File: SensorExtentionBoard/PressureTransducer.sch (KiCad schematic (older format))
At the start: 13 parts, among them J501 Conn_01x03_Male, J502 Conn_01x03_Male, J503 Conn_01x03_Male, U501 ADS1015IDGS, U502 MCP4728

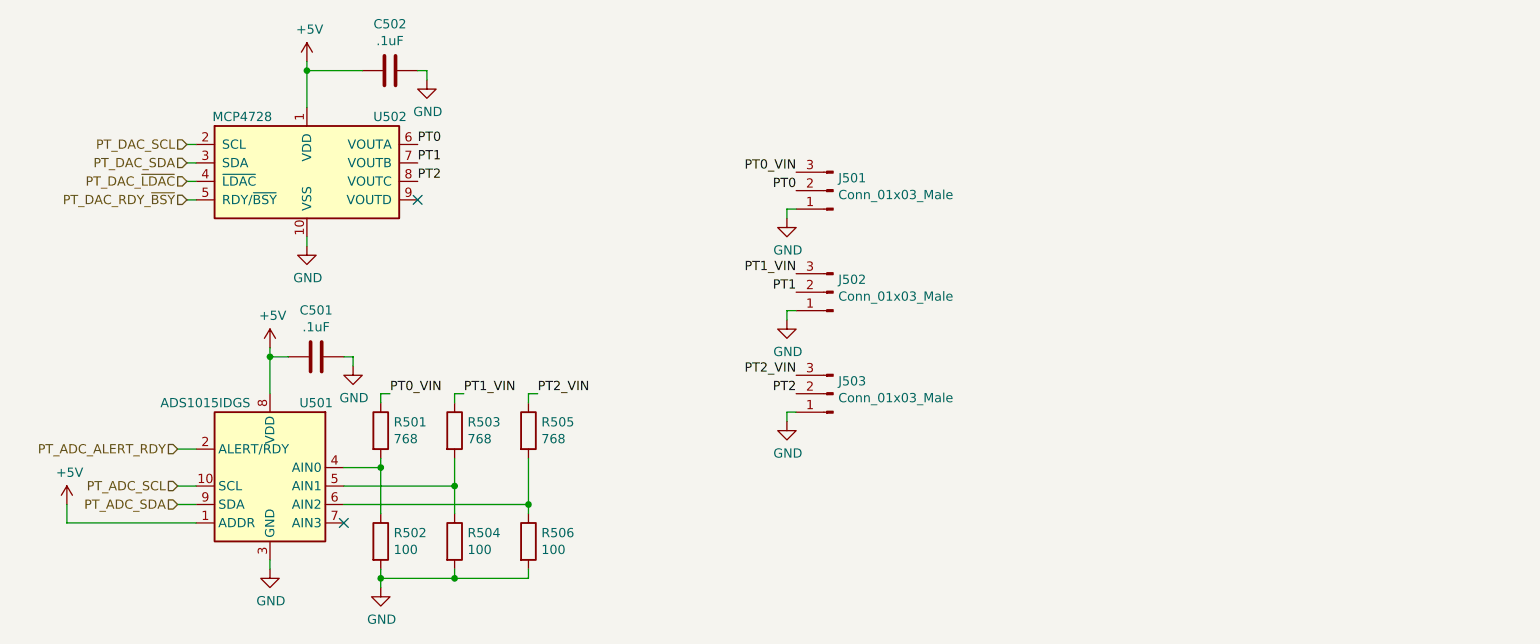
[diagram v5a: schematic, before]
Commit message: Added header for programming the EEPROM memory on the SEB
Adding this header may allow the test rig to load new memory configs
onto the SEB under test prior to running tests. This will allow
greater ability for automation of testing when the new software
requires a change to the config onboard the SEB.
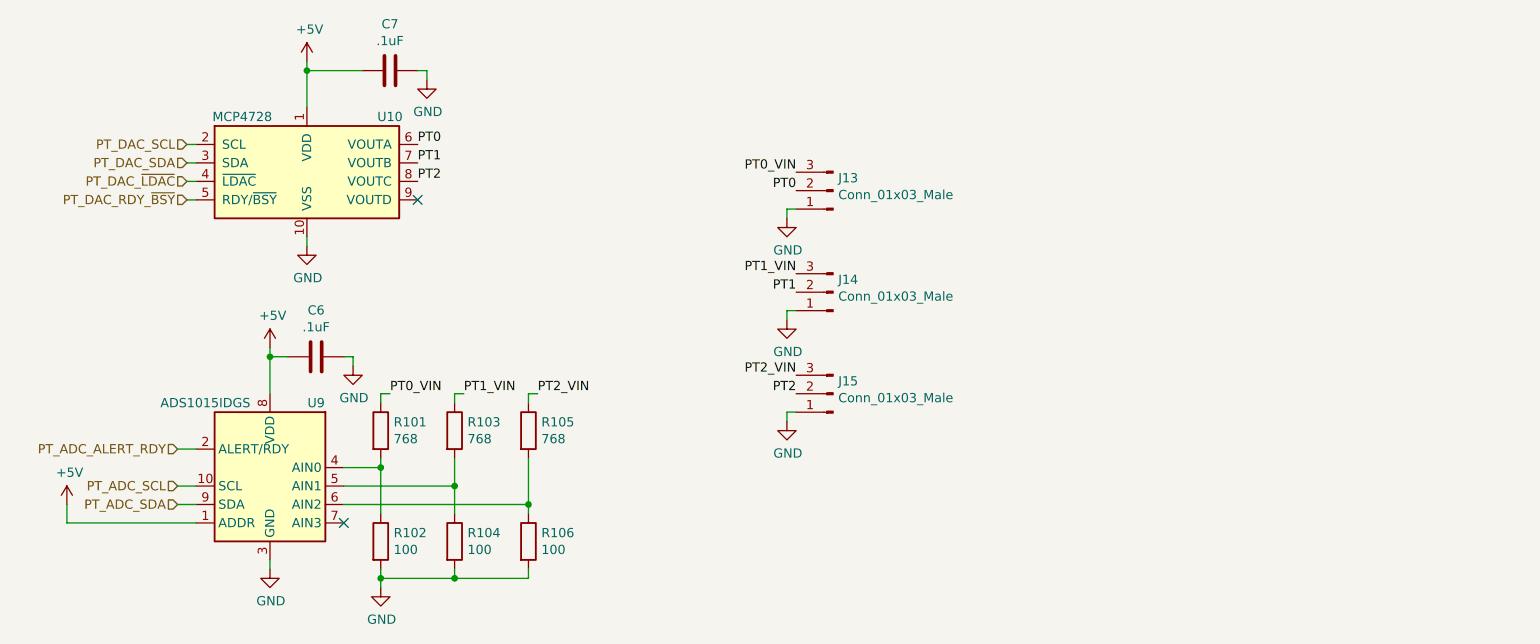
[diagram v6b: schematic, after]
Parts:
- renumbered C501 to C6, C502 to C7, J501 to J13, J502 to J14, J503 to J15, R501 to R101, R502 to R102, R503 to R103, R504 to R104, R505 to R105, R506 to R106, U502 to U10, U501 to U9
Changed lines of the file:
@@
 $EndDescr
 $Comp
-L Analog_DAC:MCP4728 U502
+L Analog_DAC:MCP4728 U10
 U 1 1 5E05A1D5
 P 4900 2900
-F 0 "U502" H 5350 3150 50  0000 C CNN
+F 0 "U10" H 5350 3150 50  0000 C CNN
 F 1 "MCP4728" H 4550 3150 50  0000 C CNN
 F 2 "Package_SO:MSOP-10_3x3mm_P0.5mm" H 4900 2300 50  0001 C CNN
@@
 $EndComp
 $Comp
-L power:+5V #PWR0504
+L power:+5V #PWR052
 U 1 1 5E05A95B
 P 4900 2350
-F 0 "#PWR0504" H 4900 2200 50  0001 C CNN
+F 0 "#PWR052" H 4900 2200 50  0001 C CNN
 F 1 "+5V" H 4915 2523 50  0000 C CNN
 F 2 "" H 4900 2350 50  0001 C CNN
@@
 	4900 2600 4900 2400
 $Comp
-L power:GND #PWR0505
+L power:GND #PWR053
 U 1 1 5E05AE1F
 P 4900 3350
-F 0 "#PWR0505" H 4900 3100 50  0001 C CNN
+F 0 "#PWR053" H 4900 3100 50  0001 C CNN
 F 1 "GND" H 4905 3177 50  0000 C CNN
 F 2 "" H 4900 3350 50  0001 C CNN
@@
 	7500 3200 7500 3150
 $Comp
-L power:GND #PWR0509
+L power:GND #PWR057
 U 1 1 5E071F60
 P 7500 3200
-F 0 "#PWR0509" H 7500 2950 50  0001 C CNN
+F 0 "#PWR057" H 7500 2950 50  0001 C CNN
 F 1 "GND" H 7505 3027 50  0000 C CNN
 F 2 "" H 7500 3200 50  0001 C CNN
@@
 	7500 3750 7500 3700
 $Comp
-L power:GND #PWR0510
+L power:GND #PWR058
 U 1 1 5E06CCB7
 P 7500 3750
-F 0 "#PWR0510" H 7500 3500 50  0001 C CNN
+F 0 "#PWR058" H 7500 3500 50  0001 C CNN
 F 1 "GND" H 7505 3577 50  0000 C CNN
 F 2 "" H 7500 3750 50  0001 C CNN
@@
 	7500 4300 7500 4250
 $Comp
-L power:GND #PWR0511
+L power:GND #PWR059
 U 1 1 5E06C38E
 P 7500 4300
-F 0 "#PWR0511" H 7500 4050 50  0001 C CNN
+F 0 "#PWR059" H 7500 4050 50  0001 C CNN
 F 1 "GND" H 7505 4127 50  0000 C CNN
 F 2 "" H 7500 4300 50  0001 C CNN
@@
 PT0
 $Comp
-L Connector:Conn_01x03_Male J503
+L Connector:Conn_01x03_Male J15
 U 1 1 5E06B5DF
 P 7750 4150
-F 0 "J503" H 7722 4082 50  0000 R CNN
+F 0 "J15" H 7722 4082 50  0000 R CNN
 F 1 "Conn_01x03_Male" H 7722 4173 50  0000 R CNN
 F 2 "Connector_Molex:Molex_MicroClasp_55932-0310_1x03_P2.00mm_Vertical" H 7750 4150 50  0001 C CNN
@@
 $EndComp
 $Comp
-L Connector:Conn_01x03_Male J502
+L Connector:Conn_01x03_Male J14
 U 1 1 5E06B2C3
 P 7750 3600
-F 0 "J502" H 7722 3532 50  0000 R CNN
+F 0 "J14" H 7722 3532 50  0000 R CNN
 F 1 "Conn_01x03_Male" H 7722 3623 50  0000 R CNN
 F 2 "Connector_Molex:Molex_MicroClasp_55932-0310_1x03_P2.00mm_Vertical" H 7750 3600 50  0001 C CNN
@@
 $EndComp
 $Comp
-L Connector:Conn_01x03_Male J501
+L Connector:Conn_01x03_Male J13
 U 1 1 5E069F3E
 P 7750 3050
-F 0 "J501" H 7722 2982 50  0000 R CNN
+F 0 "J13" H 7722 2982 50  0000 R CNN
 F 1 "Conn_01x03_Male" H 7722 3073 50  0000 R CNN
 F 2 "Connector_Molex:Molex_MicroClasp_55932-0310_1x03_P2.00mm_Vertical" H 7750 3050 50  0001 C CNN
@@
 PT2_VIN
 $Comp
-L Device:R R505
+L Device:R R105
 U 1 1 5E3D7CC3
 P 6100 4350
-F 0 "R505" H 6170 4396 50  0000 L CNN
+F 0 "R105" H 6170 4396 50  0000 L CNN
 F 1 "768" H 6170 4305 50  0000 L CNN
 F 2 "Resistor_SMD:R_1206_3216Metric_Pad1.42x1.75mm_HandSolder" V 6030 4350 50  0001 C CNN
@@
 Connection ~ 5300 4550
 $Comp
-L power:GND #PWR0503
+L power:GND #PWR051
 U 1 1 5E3D9ED4
 P 4700 5100
-F 0 "#PWR0503" H 4700 4850 50  0001 C CNN
+F 0 "#PWR051" H 4700 4850 50  0001 C CNN
 F 1 "GND" H 4705 4927 50  0000 C CNN
 F 2 "" H 4700 5100 50  0001 C CNN
@@
 $EndComp
 $Comp
-L power:GND #PWR0507
+L power:GND #PWR055
 U 1 1 5E3DACE8
 P 5300 5200
-F 0 "#PWR0507" H 5300 4950 50  0001 C CNN
+F 0 "#PWR055" H 5300 4950 50  0001 C CNN
 F 1 "GND" H 5305 5027 50  0000 C CNN
 F 2 "" H 5300 5200 50  0001 C CNN
@@
 	6100 4150 6100 4200
 $Comp
-L power:+5V #PWR0502
+L power:+5V #PWR050
 U 1 1 5E3E1CCE
 P 4700 3900
-F 0 "#PWR0502" H 4700 3750 50  0001 C CNN
+F 0 "#PWR050" H 4700 3750 50  0001 C CNN
 F 1 "+5V" H 4715 4073 50  0000 C CNN
 F 2 "" H 4700 3900 50  0001 C CNN
@@
 	4200 4450 4300 4450
 $Comp
-L power:+5V #PWR0501
+L power:+5V #PWR049
 U 1 1 5E3E9881
 P 3600 4750
-F 0 "#PWR0501" H 3600 4600 50  0001 C CNN
+F 0 "#PWR049" H 3600 4600 50  0001 C CNN
 F 1 "+5V" H 3615 4923 50  0000 C CNN
 F 2 "" H 3600 4750 50  0001 C CNN
@@
 P 5300 4950
 AR Path="/5E630276" Ref="R?"  Part="1"
-AR Path="/5E059EAC/5E630276" Ref="R502"  Part="1"
-F 0 "R502" H 5370 4996 50  0000 L CNN
+AR Path="/5E059EAC/5E630276" Ref="R102"  Part="1"
+F 0 "R102" H 5370 4996 50  0000 L CNN
 F 1 "100" H 5370 4905 50  0000 L CNN
 F 2 "Resistor_SMD:R_1206_3216Metric_Pad1.42x1.75mm_HandSolder" V 5230 4950 50  0001 C CNN
@@
 P 5700 4950
 AR Path="/5E63145E" Ref="R?"  Part="1"
-AR Path="/5E059EAC/5E63145E" Ref="R504"  Part="1"
-F 0 "R504" H 5770 4996 50  0000 L CNN
+AR Path="/5E059EAC/5E63145E" Ref="R104"  Part="1"
+F 0 "R104" H 5770 4996 50  0000 L CNN
 F 1 "100" H 5770 4905 50  0000 L CNN
 F 2 "Resistor_SMD:R_1206_3216Metric_Pad1.42x1.75mm_HandSolder" V 5630 4950 50  0001 C CNN
@@
 P 6100 4950
 AR Path="/5E631AFF" Ref="R?"  Part="1"
-AR Path="/5E059EAC/5E631AFF" Ref="R506"  Part="1"
-F 0 "R506" H 6170 4996 50  0000 L CNN
+AR Path="/5E059EAC/5E631AFF" Ref="R106"  Part="1"
+F 0 "R106" H 6170 4996 50  0000 L CNN
 F 1 "100" H 6170 4905 50  0000 L CNN
 F 2 "Resistor_SMD:R_1206_3216Metric_Pad1.42x1.75mm_HandSolder" V 6030 4950 50  0001 C CNN
@@
 $EndComp
 $Comp
-L Device:R R503
+L Device:R R103
 U 1 1 5E639E33
 P 5700 4350
-F 0 "R503" H 5770 4396 50  0000 L CNN
+F 0 "R103" H 5770 4396 50  0000 L CNN
 F 1 "768" H 5770 4305 50  0000 L CNN
 F 2 "Resistor_SMD:R_1206_3216Metric_Pad1.42x1.75mm_HandSolder" V 5630 4350 50  0001 C CNN
@@
 $EndComp
 $Comp
-L Device:R R501
+L Device:R R101
 U 1 1 5E639FAD
 P 5300 4350
-F 0 "R501" H 5370 4396 50  0000 L CNN
+F 0 "R101" H 5370 4396 50  0000 L CNN
 F 1 "768" H 5370 4305 50  0000 L CNN
 F 2 "Resistor_SMD:R_1206_3216Metric_Pad1.42x1.75mm_HandSolder" V 5230 4350 50  0001 C CNN
@@
 P 5350 2400
 AR Path="/5E13E0B3" Ref="C?"  Part="1"
-AR Path="/5E059EAC/5E13E0B3" Ref="C502"  Part="1"
-F 0 "C502" V 5098 2400 50  0000 C CNN
+AR Path="/5E059EAC/5E13E0B3" Ref="C7"  Part="1"
+F 0 "C7" V 5098 2400 50  0000 C CNN
 F 1 ".1uF" V 5189 2400 50  0000 C CNN
 F 2 "" H 5388 2250 50  0001 C CNN
@@
 P 5550 2450
 AR Path="/5E13E0B9" Ref="#PWR?"  Part="1"
-AR Path="/5E059EAC/5E13E0B9" Ref="#PWR0508"  Part="1"
-F 0 "#PWR0508" H 5550 2200 50  0001 C CNN
+AR Path="/5E059EAC/5E13E0B9" Ref="#PWR056"  Part="1"
+F 0 "#PWR056" H 5550 2200 50  0001 C CNN
 F 1 "GND" H 5555 2277 50  0000 C CNN
 F 2 "" H 5550 2450 50  0001 C CNN
@@
 P 4950 3950
 AR Path="/5E1425A7" Ref="C?"  Part="1"
-AR Path="/5E059EAC/5E1425A7" Ref="C501"  Part="1"
-F 0 "C501" V 4698 3950 50  0000 C CNN
+AR Path="/5E059EAC/5E1425A7" Ref="C6"  Part="1"
+F 0 "C6" V 4698 3950 50  0000 C CNN
 F 1 ".1uF" V 4789 3950 50  0000 C CNN
 F 2 "" H 4988 3800 50  0001 C CNN
@@
 P 5150 4000
 AR Path="/5E1425AD" Ref="#PWR?"  Part="1"
-AR Path="/5E059EAC/5E1425AD" Ref="#PWR0506"  Part="1"
-F 0 "#PWR0506" H 5150 3750 50  0001 C CNN
+AR Path="/5E059EAC/5E1425AD" Ref="#PWR054"  Part="1"
+F 0 "#PWR054" H 5150 3750 50  0001 C CNN
 F 1 "GND" H 5155 3827 50  0000 C CNN
 F 2 "" H 5150 4000 50  0001 C CNN
@@
 	4700 3950 4700 4150
 $Comp
-L Analog_ADC:ADS1015IDGS U501
+L Analog_ADC:ADS1015IDGS U9
 U 1 1 5E1F9CD6
 P 4700 4650
-F 0 "U501" H 4450 5100 50  0000 C CNN
+F 0 "U9" H 4450 5100 50  0000 C CNN
 F 1 "ADS1015IDGS" H 5050 5100 50  0000 C CNN
 F 2 "Package_SO:TSSOP-10_3x3mm_P0.5mm" H 4700 4150 50  0001 C CNN

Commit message: Changed component footprints to conform to RP standard components
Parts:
- C6, C7: footprint (none) -> Capacitor_SMD:C_1206_3216Metric_Pad1.42x1.75mm_HandSolder
- J13, J14, J15: footprint Connector_Molex:Molex_MicroClasp_55932-0310_1x03_P2.00mm_Vertical -> Connector_Molex:Molex_MicroClasp_55932-0330_1x03_P2.00mm_Vertical
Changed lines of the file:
@@
 encoding utf-8
 Sheet 5 5
-Title ""
-Date ""
-Rev ""
-Comp ""
-Comment1 ""
+Title "Helix Test Rig SEB"
+Date "2020-01-14"
+Rev "1.0.0"
+Comp "SDSU Rocket Project"
+Comment1 "Schematic Design: David Knight"
 Comment2 ""
 Comment3 ""
@@
 $EndComp
 $Comp
-L power:+5V #PWR052
+L power:+5V #PWR055
 U 1 1 5E05A95B
 P 4900 2350
-F 0 "#PWR052" H 4900 2200 50  0001 C CNN
+F 0 "#PWR055" H 4900 2200 50  0001 C CNN
 F 1 "+5V" H 4915 2523 50  0000 C CNN
 F 2 "" H 4900 2350 50  0001 C CNN
@@
 	4900 2600 4900 2400
 $Comp
-L power:GND #PWR053
+L power:GND #PWR056
 U 1 1 5E05AE1F
 P 4900 3350
-F 0 "#PWR053" H 4900 3100 50  0001 C CNN
+F 0 "#PWR056" H 4900 3100 50  0001 C CNN
 F 1 "GND" H 4905 3177 50  0000 C CNN
 F 2 "" H 4900 3350 50  0001 C CNN
@@
 	7500 3200 7500 3150
 $Comp
-L power:GND #PWR057
+L power:GND #PWR060
 U 1 1 5E071F60
 P 7500 3200
-F 0 "#PWR057" H 7500 2950 50  0001 C CNN
+F 0 "#PWR060" H 7500 2950 50  0001 C CNN
 F 1 "GND" H 7505 3027 50  0000 C CNN
 F 2 "" H 7500 3200 50  0001 C CNN
@@
 	7500 3750 7500 3700
 $Comp
-L power:GND #PWR058
+L power:GND #PWR061
 U 1 1 5E06CCB7
 P 7500 3750
-F 0 "#PWR058" H 7500 3500 50  0001 C CNN
+F 0 "#PWR061" H 7500 3500 50  0001 C CNN
 F 1 "GND" H 7505 3577 50  0000 C CNN
 F 2 "" H 7500 3750 50  0001 C CNN
@@
 	7500 4300 7500 4250
 $Comp
-L power:GND #PWR059
+L power:GND #PWR062
 U 1 1 5E06C38E
 P 7500 4300
-F 0 "#PWR059" H 7500 4050 50  0001 C CNN
+F 0 "#PWR062" H 7500 4050 50  0001 C CNN
 F 1 "GND" H 7505 4127 50  0000 C CNN
 F 2 "" H 7500 4300 50  0001 C CNN
@@
 F 0 "J15" H 7722 4082 50  0000 R CNN
 F 1 "Conn_01x03_Male" H 7722 4173 50  0000 R CNN
-F 2 "Connector_Molex:Molex_MicroClasp_55932-0310_1x03_P2.00mm_Vertical" H 7750 4150 50  0001 C CNN
+F 2 "Connector_Molex:Molex_MicroClasp_55932-0330_1x03_P2.00mm_Vertical" H 7750 4150 50  0001 C CNN
 F 3 "~" H 7750 4150 50  0001 C CNN
 	1    7750 4150
@@
 F 0 "J14" H 7722 3532 50  0000 R CNN
 F 1 "Conn_01x03_Male" H 7722 3623 50  0000 R CNN
-F 2 "Connector_Molex:Molex_MicroClasp_55932-0310_1x03_P2.00mm_Vertical" H 7750 3600 50  0001 C CNN
+F 2 "Connector_Molex:Molex_MicroClasp_55932-0330_1x03_P2.00mm_Vertical" H 7750 3600 50  0001 C CNN
 F 3 "~" H 7750 3600 50  0001 C CNN
 	1    7750 3600
@@
 F 0 "J13" H 7722 2982 50  0000 R CNN
 F 1 "Conn_01x03_Male" H 7722 3073 50  0000 R CNN
-F 2 "Connector_Molex:Molex_MicroClasp_55932-0310_1x03_P2.00mm_Vertical" H 7750 3050 50  0001 C CNN
+F 2 "Connector_Molex:Molex_MicroClasp_55932-0330_1x03_P2.00mm_Vertical" H 7750 3050 50  0001 C CNN
 F 3 "~" H 7750 3050 50  0001 C CNN
 	1    7750 3050
@@
 Connection ~ 5300 4550
 $Comp
-L power:GND #PWR051
+L power:GND #PWR054
 U 1 1 5E3D9ED4
 P 4700 5100
-F 0 "#PWR051" H 4700 4850 50  0001 C CNN
+F 0 "#PWR054" H 4700 4850 50  0001 C CNN
 F 1 "GND" H 4705 4927 50  0000 C CNN
 F 2 "" H 4700 5100 50  0001 C CNN
@@
 $EndComp
 $Comp
-L power:GND #PWR055
+L power:GND #PWR058
 U 1 1 5E3DACE8
 P 5300 5200
-F 0 "#PWR055" H 5300 4950 50  0001 C CNN
+F 0 "#PWR058" H 5300 4950 50  0001 C CNN
 F 1 "GND" H 5305 5027 50  0000 C CNN
 F 2 "" H 5300 5200 50  0001 C CNN
@@
 	6100 4150 6100 4200
 $Comp
-L power:+5V #PWR050
+L power:+5V #PWR053
 U 1 1 5E3E1CCE
 P 4700 3900
-F 0 "#PWR050" H 4700 3750 50  0001 C CNN
+F 0 "#PWR053" H 4700 3750 50  0001 C CNN
 F 1 "+5V" H 4715 4073 50  0000 C CNN
 F 2 "" H 4700 3900 50  0001 C CNN
@@
 	4200 4450 4300 4450
 $Comp
-L power:+5V #PWR049
+L power:+5V #PWR052
 U 1 1 5E3E9881
 P 3600 4750
-F 0 "#PWR049" H 3600 4600 50  0001 C CNN
+F 0 "#PWR052" H 3600 4600 50  0001 C CNN
 F 1 "+5V" H 3615 4923 50  0000 C CNN
 F 2 "" H 3600 4750 50  0001 C CNN
@@
 F 0 "C7" V 5098 2400 50  0000 C CNN
 F 1 ".1uF" V 5189 2400 50  0000 C CNN
-F 2 "" H 5388 2250 50  0001 C CNN
+F 2 "Capacitor_SMD:C_1206_3216Metric_Pad1.42x1.75mm_HandSolder" H 5388 2250 50  0001 C CNN
 F 3 "~" H 5350 2400 50  0001 C CNN
 	1    5350 2400
@@
 P 5550 2450
 AR Path="/5E13E0B9" Ref="#PWR?"  Part="1"
-AR Path="/5E059EAC/5E13E0B9" Ref="#PWR056"  Part="1"
-F 0 "#PWR056" H 5550 2200 50  0001 C CNN
+AR Path="/5E059EAC/5E13E0B9" Ref="#PWR059"  Part="1"
+F 0 "#PWR059" H 5550 2200 50  0001 C CNN
 F 1 "GND" H 5555 2277 50  0000 C CNN
 F 2 "" H 5550 2450 50  0001 C CNN
@@
 F 0 "C6" V 4698 3950 50  0000 C CNN
 F 1 ".1uF" V 4789 3950 50  0000 C CNN
-F 2 "" H 4988 3800 50  0001 C CNN
+F 2 "Capacitor_SMD:C_1206_3216Metric_Pad1.42x1.75mm_HandSolder" H 4988 3800 50  0001 C CNN
 F 3 "~" H 4950 3950 50  0001 C CNN
 	1    4950 3950
@@
 P 5150 4000
 AR Path="/5E1425AD" Ref="#PWR?"  Part="1"
-AR Path="/5E059EAC/5E1425AD" Ref="#PWR054"  Part="1"
-F 0 "#PWR054" H 5150 3750 50  0001 C CNN
+AR Path="/5E059EAC/5E1425AD" Ref="#PWR057"  Part="1"
+F 0 "#PWR057" H 5150 3750 50  0001 C CNN
 F 1 "GND" H 5155 3827 50  0000 C CNN
 F 2 "" H 5150 4000 50  0001 C CNN
